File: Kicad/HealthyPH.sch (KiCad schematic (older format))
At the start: 13 parts, among them P1 CONN_8

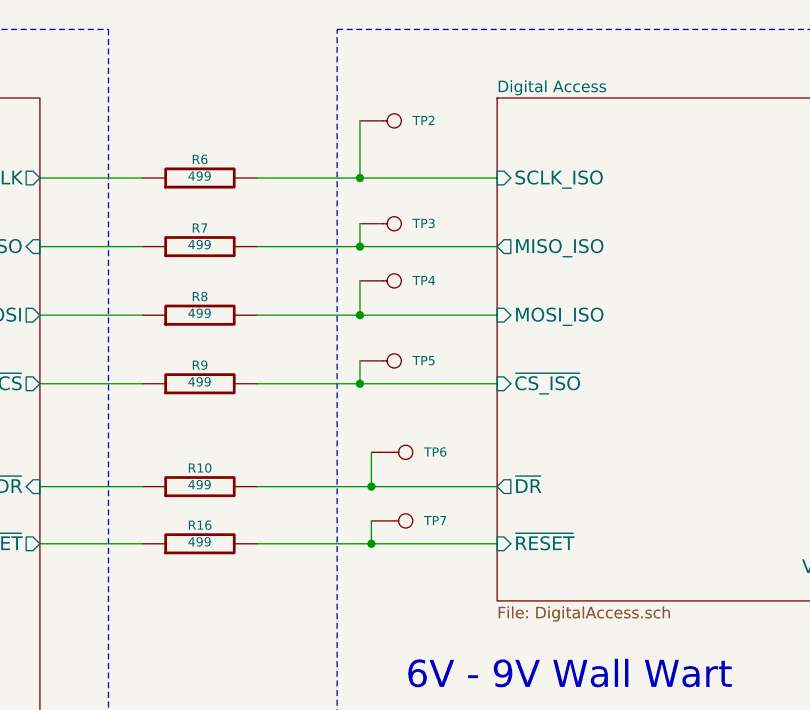
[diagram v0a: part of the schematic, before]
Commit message: updated with changes for pH volt testing in mcp3901
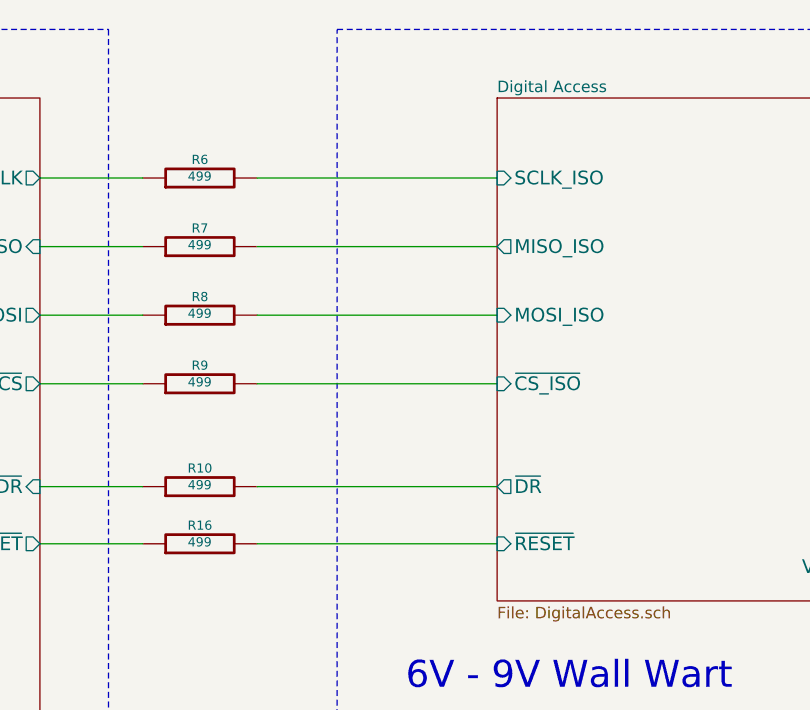
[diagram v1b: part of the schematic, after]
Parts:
- removed TP2, TP3, TP4, TP5, TP6, TP7: CONN_1, symbol CONN_1
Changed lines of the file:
@@
 Sheet 1 7
 Title ""
-Date "15 sep 2014"
+Date "11 oct 2014"
 Rev ""
 Comp ""
@@
 	1    0    0    -1
 $EndComp
-$Comp
-L CONN_1 TP2
-U 1 1 53F5DD37
-P 4250 1000
-F 0 "TP2" H 4330 1000 40  0000 L CNN
-F 1 "CONN_1" H 4250 1055 30  0001 C CNN
-F 2 "" H 4250 1000 60  0000 C CNN
-F 3 "" H 4250 1000 60  0000 C CNN
-	1    4250 1000
-	1    0    0    -1
-$EndComp
-$Comp
-L CONN_1 TP3
-U 1 1 53F5DE71
-P 4250 1450
-F 0 "TP3" H 4330 1450 40  0000 L CNN
-F 1 "CONN_1" H 4250 1505 30  0001 C CNN
-F 2 "" H 4250 1450 60  0000 C CNN
-F 3 "" H 4250 1450 60  0000 C CNN
-	1    4250 1450
-	1    0    0    -1
-$EndComp
-$Comp
-L CONN_1 TP4
-U 1 1 53F5DF29
-P 4250 1700
-F 0 "TP4" H 4330 1700 40  0000 L CNN
-F 1 "CONN_1" H 4250 1755 30  0001 C CNN
-F 2 "" H 4250 1700 60  0000 C CNN
-F 3 "" H 4250 1700 60  0000 C CNN
-	1    4250 1700
-	1    0    0    -1
-$EndComp
-$Comp
-L CONN_1 TP5
-U 1 1 53F5DFE3
-P 4250 2050
-F 0 "TP5" H 4330 2050 40  0000 L CNN
-F 1 "CONN_1" H 4250 2105 30  0001 C CNN
-F 2 "" H 4250 2050 60  0000 C CNN
-F 3 "" H 4250 2050 60  0000 C CNN
-	1    4250 2050
-	1    0    0    -1
-$EndComp
-$Comp
-L CONN_1 TP6
-U 1 1 53F5E09F
-P 4300 2450
-F 0 "TP6" H 4380 2450 40  0000 L CNN
-F 1 "CONN_1" H 4300 2505 30  0001 C CNN
-F 2 "" H 4300 2450 60  0000 C CNN
-F 3 "" H 4300 2450 60  0000 C CNN
-	1    4300 2450
-	1    0    0    -1
-$EndComp
-$Comp
-L CONN_1 TP7
-U 1 1 53F5E15D
-P 4300 2750
-F 0 "TP7" H 4380 2750 40  0000 L CNN
-F 1 "CONN_1" H 4300 2805 30  0001 C CNN
-F 2 "" H 4300 2750 60  0000 C CNN
-F 3 "" H 4300 2750 60  0000 C CNN
-	1    4300 2750
-	1    0    0    -1
-$EndComp
 Wire Wire Line
 	6650 1000 7250 1000
@@
 Wire Wire Line
 	7250 1400 6800 1400
-Wire Wire Line
-	4100 1000 4100 1250
-Connection ~ 4100 1250
-Wire Wire Line
-	4100 1450 4100 1550
-Connection ~ 4100 1550
-Wire Wire Line
-	4100 1700 4100 1850
-Connection ~ 4100 1850
-Wire Wire Line
-	4100 2050 4100 2150
-Connection ~ 4100 2150
-Wire Wire Line
-	4150 2450 4150 2600
-Connection ~ 4150 2600
-Wire Wire Line
-	4150 2750 4150 2850
 Wire Wire Line
 	10150 2600 10150 1400
@@
 Wire Wire Line
 	3650 2850 4700 2850
-Connection ~ 4150 2850
 Wire Wire Line
 	6800 2600 10150 2600

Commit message: Ready for Rev3 First layout review
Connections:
- net Digital Access/V+_WallWart: now also P1.3 (P3); no longer P1.4 (P4)
- net Temperature/10K Therm: now also P1.4 (P4); no longer P1.3 (P3)
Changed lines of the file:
@@
 Sheet 1 7
 Title ""
-Date "11 oct 2014"
+Date "18 oct 2014"
 Rev ""
 Comp ""
@@
 	9150 2150 10000 2150
 Wire Wire Line
-	10000 2150 10000 1300
-Wire Wire Line
-	10000 1300 10700 1300
-Wire Wire Line
 	10300 1500 10300 4000
 Wire Wire Line
@@
 	7250 1400 6800 1400
 Wire Wire Line
-	10150 2600 10150 1400
-Wire Wire Line
-	10150 1400 10700 1400
+	10150 1300 10150 2600
 $Sheet
 S 7250 800  1900 700
@@
 	3650 2850 4700 2850
 Wire Wire Line
-	6800 2600 10150 2600
+	10150 2600 6800 2600
 Connection ~ 6800 2600
+Wire Wire Line
+	10150 1300 10700 1300
+Wire Wire Line
+	10700 1400 10000 1400
+Wire Wire Line
+	10000 1400 10000 2150
 $EndSCHEMATC

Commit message: updated based on feedback. Ready for second review
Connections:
- net Digital Access/V+_WallWart: no longer P1.3 (P3)
- net Temperature/10K Therm: now also P1.3 (P3); no longer P1.4 (P4)
- net pH/pH_Probe_GND: now also P1.1 (P1); no longer P1.2 (P2)
- net pH/pH_Probe_V: now also P1.2 (P2); no longer P1.1 (P1)
- new net Temperature/V+_WallWart_Out: P1.4 (P4)
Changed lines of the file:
@@
 Sheet 1 7
 Title ""
-Date "18 oct 2014"
+Date "21 oct 2014"
 Rev ""
 Comp ""
@@
 F1 "WallWart.sch" 50
 F2 "V+_WallWart" O L 7250 3150 60
-$EndSheet
-$Sheet
-S 800  900  1900 3900
-U 53DCD805
-F0 "Arduino" 50
-F1 "Arduino.sch" 50
-F2 "SCLK" O R 2700 1250 60
-F3 "MISO" I R 2700 1550 60
-F4 "MOSI" O R 2700 1850 60
-F5 "~CS" O R 2700 2150 60
-F6 "~RESET" O R 2700 2850 60
-F7 "~DR" I R 2700 2600 60
-F8 "V+_ARD" O R 2700 3900 60
-F9 "GND_ARD" I R 2700 4100 60
-F10 "PumpUp" O R 2700 4350 60
-F11 "PumpDown" O R 2700 4600 60
 $EndSheet
 Text Notes 2900 4900 0    118  ~ 0
@@
 F3 "Therm+" O L 7250 2050 60
 F4 "Therm-" O L 7250 2200 60
+F5 "V+_WallWart" I L 7250 2350 60
+F6 "V+_WallWart_Out" O R 9150 2350 60
 $EndSheet
 $Sheet
@@
 	3650 2600 4700 2600
 Wire Wire Line
-	9150 1200 10700 1200
-Wire Wire Line
-	9150 2150 10000 2150
+	10000 2150 9150 2150
 Wire Wire Line
 	10300 1500 10300 4000
@@
 Wire Wire Line
 	7250 1400 6800 1400
-Wire Wire Line
-	10150 1300 10150 2600
 $Sheet
 S 7250 800  1900 700
@@
 F3 "ph_ADC_IN+" I L 7250 1000 60
 F4 "pH_ADC_IN-" I L 7250 1200 60
-F5 "pH_Probe_V" I R 9150 1000 60
-F6 "pH_Probe_GND" I R 9150 1200 60
-$EndSheet
-Wire Wire Line
-	9150 1000 10600 1000
-Wire Wire Line
-	10600 1000 10600 1100
-Wire Wire Line
-	10600 1100 10700 1100
+F5 "pH_Probe_V" I R 9150 1200 60
+F6 "pH_Probe_GND" I R 9150 1000 60
+$EndSheet
 $Sheet
 S 4700 900  1950 2200
@@
 	3650 2850 4700 2850
 Wire Wire Line
-	10150 2600 6800 2600
-Connection ~ 6800 2600
-Wire Wire Line
-	10150 1300 10700 1300
-Wire Wire Line
-	10700 1400 10000 1400
-Wire Wire Line
-	10000 1400 10000 2150
+	10100 2350 9150 2350
+Wire Wire Line
+	7250 2350 6800 2350
+Connection ~ 6800 2350
+Wire Wire Line
+	9150 1200 10700 1200
+Wire Wire Line
+	9150 1000 10450 1000
+Wire Wire Line
+	10100 2350 10100 1400
+Wire Wire Line
+	10100 1400 10700 1400
+Wire Wire Line
+	10000 2150 10000 1300
+Wire Wire Line
+	10000 1300 10700 1300
+Wire Wire Line
+	10450 1000 10450 1100
+Wire Wire Line
+	10450 1100 10700 1100
+$Sheet
+S 800  900  1900 3900
+U 53DCD805
+F0 "Arduino" 50
+F1 "Arduino.sch" 50
+F2 "SCLK" O R 2700 1250 60
+F3 "MISO" I R 2700 1550 60
+F4 "MOSI" O R 2700 1850 60
+F5 "~CS" O R 2700 2150 60
+F6 "V+_ARD" O R 2700 3900 60
+F7 "GND_ARD" I R 2700 4100 60
+F8 "PumpUp" O R 2700 4350 60
+F9 "PumpDown" O R 2700 4600 60
+F10 "~RESET" O R 2700 2850 60
+F11 "~DR" I R 2700 2600 60
+$EndSheet
 $EndSCHEMATC

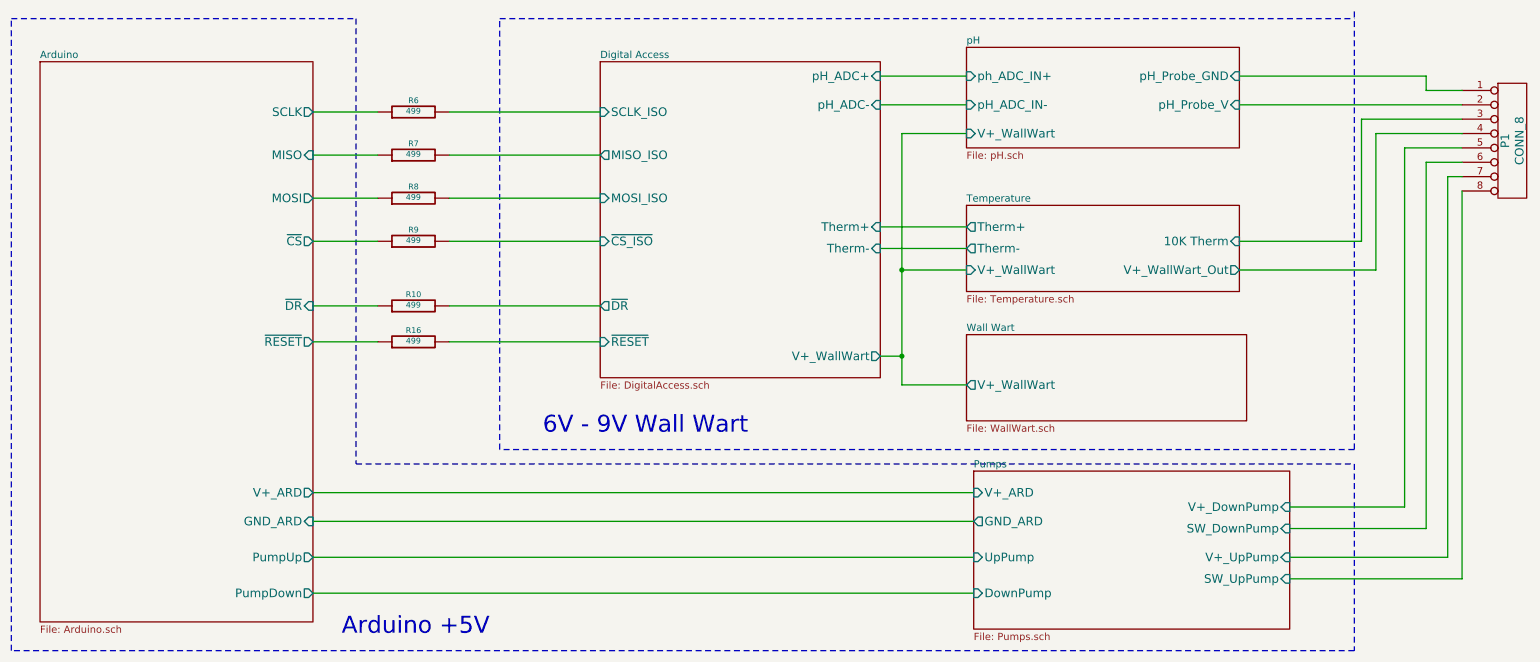
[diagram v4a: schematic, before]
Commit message: first pass changing ADC
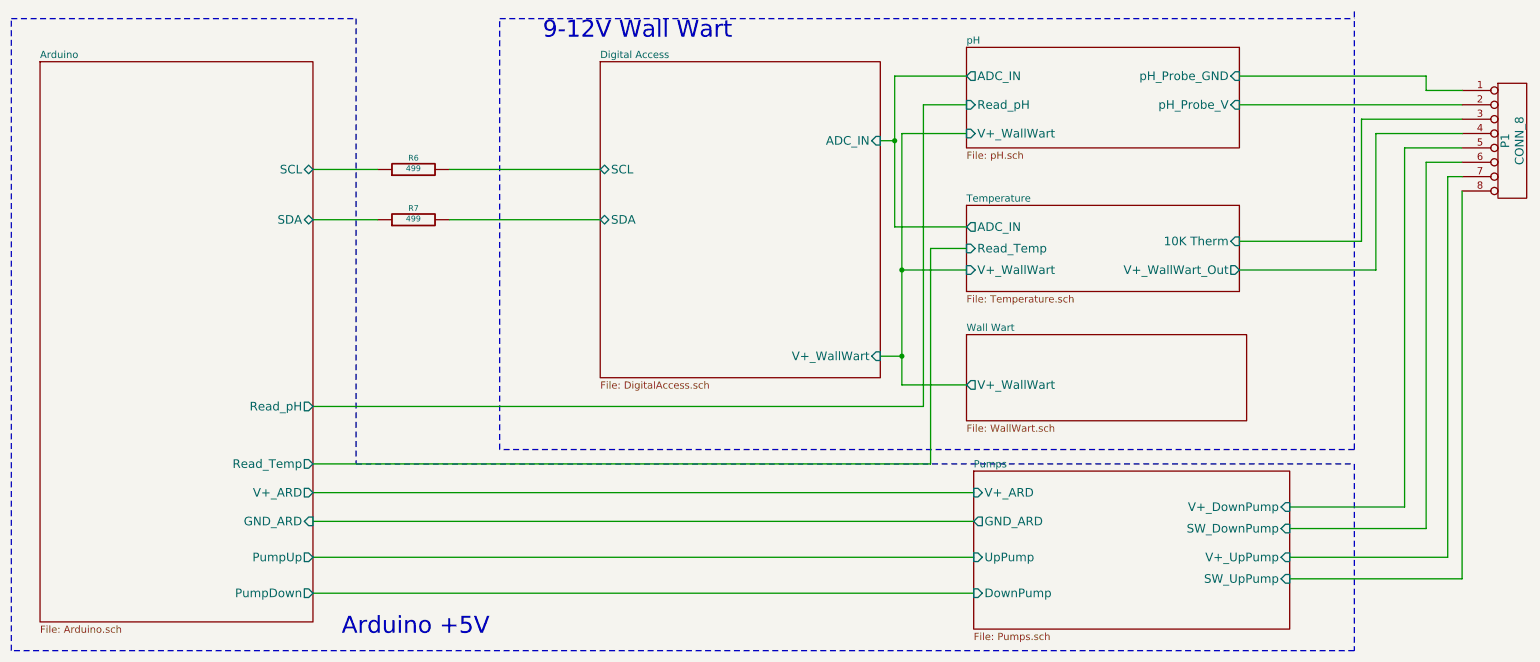
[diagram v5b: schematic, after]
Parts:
- removed R10, R16, R8, R9: 499, ~, symbol R
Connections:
- net Arduino/MISO renamed Arduino/SDA
- net Arduino/SCLK renamed Arduino/SCL
- net Digital Access/MISO_ISO renamed Digital Access/SDA
- net Digital Access/SCLK_ISO renamed Digital Access/SCL
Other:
- note added: "9-12V Wall Wart"
- note removed: "6V - 9V Wall Wart"
- moved on the sheet: R6, R7
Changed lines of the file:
@@
 Sheet 1 7
 Title ""
-Date "10 nov 2014"
+Date "11 nov 2014"
 Rev ""
 Comp ""
@@
 Text Notes 2900 4900 0    118  ~ 0
 Arduino +5V
-Text Notes 4300 3500 0    118  ~ 0
-6V - 9V Wall Wart
+Text Notes 4300 750  0    118  ~ 0
+9-12V Wall Wart
 $Comp
 L R R6
 U 1 1 53E4B553
-P 3400 1250
-F 0 "R6" V 3480 1250 40  0000 C CNN
-F 1 "499" V 3407 1251 40  0000 C CNN
-F 2 "~" V 3330 1250 30  0000 C CNN
-F 3 "~" H 3400 1250 30  0000 C CNN
-	1    3400 1250
+P 3400 1650
+F 0 "R6" V 3480 1650 40  0000 C CNN
+F 1 "499" V 3407 1651 40  0000 C CNN
+F 2 "~" V 3330 1650 30  0000 C CNN
+F 3 "~" H 3400 1650 30  0000 C CNN
+	1    3400 1650
 	0    -1   -1   0
 $EndComp
@@
 L R R7
 U 1 1 53E4B560
-P 3400 1550
-F 0 "R7" V 3480 1550 40  0000 C CNN
-F 1 "499" V 3407 1551 40  0000 C CNN
-F 2 "~" V 3330 1550 30  0000 C CNN
-F 3 "~" H 3400 1550 30  0000 C CNN
-	1    3400 1550
-	0    -1   -1   0
-$EndComp
-$Comp
-L R R8
-U 1 1 53E4B566
-P 3400 1850
-F 0 "R8" V 3480 1850 40  0000 C CNN
-F 1 "499" V 3407 1851 40  0000 C CNN
-F 2 "~" V 3330 1850 30  0000 C CNN
-F 3 "~" H 3400 1850 30  0000 C CNN
-	1    3400 1850
-	0    -1   -1   0
-$EndComp
-$Comp
-L R R9
-U 1 1 53E4B56C
-P 3400 2150
-F 0 "R9" V 3480 2150 40  0000 C CNN
-F 1 "499" V 3407 2151 40  0000 C CNN
-F 2 "~" V 3330 2150 30  0000 C CNN
-F 3 "~" H 3400 2150 30  0000 C CNN
-	1    3400 2150
-	0    -1   -1   0
-$EndComp
-$Comp
-L R R10
-U 1 1 53E4B572
-P 3400 2600
-F 0 "R10" V 3480 2600 40  0000 C CNN
-F 1 "499" V 3407 2601 40  0000 C CNN
-F 2 "~" V 3330 2600 30  0000 C CNN
-F 3 "~" H 3400 2600 30  0000 C CNN
-	1    3400 2600
+P 3400 2000
+F 0 "R7" V 3480 2000 40  0000 C CNN
+F 1 "499" V 3407 2001 40  0000 C CNN
+F 2 "~" V 3330 2000 30  0000 C CNN
+F 3 "~" H 3400 2000 30  0000 C CNN
+	1    3400 2000
 	0    -1   -1   0
 $EndComp
@@
 F1 "Temperature.sch" 50
 F2 "10K Therm" I R 9150 2150 60
-F3 "Therm+" O L 7250 2050 60
-F4 "Therm-" O L 7250 2200 60
-F5 "V+_WallWart" I L 7250 2350 60
-F6 "V+_WallWart_Out" O R 9150 2350 60
+F3 "V+_WallWart" I L 7250 2350 60
+F4 "V+_WallWart_Out" O R 9150 2350 60
+F5 "ADC_IN" O L 7250 2050 60
+F6 "Read_Temp" I L 7250 2200 60
 $EndSheet
 $Sheet
@@
 $EndComp
 Wire Wire Line
-	6650 1000 7250 1000
-Wire Wire Line
-	6650 1200 7250 1200
-Wire Wire Line
 	6800 1400 6800 3150
 Wire Wire Line
@@
 	600  600  3000 600
 Wire Wire Line
-	3650 1250 4700 1250
-Wire Wire Line
-	3650 1550 4700 1550
-Wire Wire Line
-	3650 1850 4700 1850
-Wire Wire Line
-	3650 2150 4700 2150
-Wire Wire Line
-	3650 2600 4700 2600
+	3650 1650 4700 1650
+Wire Wire Line
+	3650 2000 4700 2000
 Wire Wire Line
 	10000 2150 9150 2150
@@
 	10700 4500 9500 4500
 Wire Wire Line
-	3150 1250 2700 1250
-Wire Wire Line
-	3150 1550 2700 1550
-Wire Wire Line
-	2700 1850 3150 1850
-Wire Wire Line
-	3150 2150 2700 2150
-Wire Wire Line
-	2700 2600 3150 2600
+	3150 1650 2700 1650
+Wire Wire Line
+	3150 2000 2700 2000
 Wire Wire Line
 	7250 1400 6800 1400
@@
 F1 "pH.sch" 50
 F2 "V+_WallWart" I L 7250 1400 60
-F3 "ph_ADC_IN+" I L 7250 1000 60
-F4 "pH_ADC_IN-" I L 7250 1200 60
-F5 "pH_Probe_V" I R 9150 1200 60
-F6 "pH_Probe_GND" I R 9150 1000 60
+F3 "pH_Probe_V" I R 9150 1200 60
+F4 "pH_Probe_GND" I R 9150 1000 60
+F5 "ADC_IN" O L 7250 1000 60
+F6 "Read_pH" I L 7250 1200 60
+$EndSheet
+Wire Wire Line
+	10100 2350 9150 2350
+Wire Wire Line
+	7250 2350 6800 2350
+Connection ~ 6800 2350
+Wire Wire Line
+	9150 1200 10700 1200
+Wire Wire Line
+	9150 1000 10450 1000
+Wire Wire Line
+	10100 2350 10100 1400
+Wire Wire Line
+	10100 1400 10700 1400
+Wire Wire Line
+	10000 2150 10000 1300
+Wire Wire Line
+	10000 1300 10700 1300
+Wire Wire Line
+	10450 1000 10450 1100
+Wire Wire Line
+	10450 1100 10700 1100
+$Sheet
+S 800  900  1900 3900
+U 53DCD805
+F0 "Arduino" 50
+F1 "Arduino.sch" 50
+F2 "V+_ARD" O R 2700 3900 60
+F3 "GND_ARD" I R 2700 4100 60
+F4 "PumpUp" O R 2700 4350 60
+F5 "PumpDown" O R 2700 4600 60
+F6 "SDA" B R 2700 2000 60
+F7 "SCL" B R 2700 1650 60
+F8 "Read_pH" O R 2700 3300 60
+F9 "Read_Temp" O R 2700 3700 60
 $EndSheet
 $Sheet
@@
 F0 "Digital Access" 50
 F1 "DigitalAccess.sch" 50
-F2 "~RESET" I L 4700 2850 60
-F3 "~DR" O L 4700 2600 60
-F4 "pH_ADC+" I R 6650 1000 60
-F5 "pH_ADC-" I R 6650 1200 60
-F6 "V+_WallWart" O R 6650 2950 60
-F7 "MOSI_ISO" I L 4700 1850 60
-F8 "MISO_ISO" O L 4700 1550 60
-F9 "SCLK_ISO" I L 4700 1250 60
-F10 "~CS_ISO" I L 4700 2150 60
-F11 "Therm+" I R 6650 2050 60
-F12 "Therm-" I R 6650 2200 60
-$EndSheet
-Wire Wire Line
-	6650 2200 7250 2200
-Wire Wire Line
-	6650 2050 7250 2050
-$Comp
-L R R16
-U 1 1 54142348
-P 3400 2850
-F 0 "R16" V 3480 2850 40  0000 C CNN
-F 1 "499" V 3407 2851 40  0000 C CNN
-F 2 "~" V 3330 2850 30  0000 C CNN
-F 3 "~" H 3400 2850 30  0000 C CNN
-	1    3400 2850
-	0    -1   -1   0
-$EndComp
-Wire Wire Line
-	2700 2850 3150 2850
-Wire Wire Line
-	3650 2850 4700 2850
-Wire Wire Line
-	10100 2350 9150 2350
-Wire Wire Line
-	7250 2350 6800 2350
-Connection ~ 6800 2350
-Wire Wire Line
-	9150 1200 10700 1200
-Wire Wire Line
-	9150 1000 10450 1000
-Wire Wire Line
-	10100 2350 10100 1400
-Wire Wire Line
-	10100 1400 10700 1400
-Wire Wire Line
-	10000 2150 10000 1300
-Wire Wire Line
-	10000 1300 10700 1300
-Wire Wire Line
-	10450 1000 10450 1100
-Wire Wire Line
-	10450 1100 10700 1100
-$Sheet
-S 800  900  1900 3900
-U 53DCD805
-F0 "Arduino" 50
-F1 "Arduino.sch" 50
-F2 "SCLK" O R 2700 1250 60
-F3 "MISO" I R 2700 1550 60
-F4 "MOSI" O R 2700 1850 60
-F5 "~CS" O R 2700 2150 60
-F6 "V+_ARD" O R 2700 3900 60
-F7 "GND_ARD" I R 2700 4100 60
-F8 "PumpUp" O R 2700 4350 60
-F9 "PumpDown" O R 2700 4600 60
-F10 "~RESET" O R 2700 2850 60
-F11 "~DR" I R 2700 2600 60
-$EndSheet
+F2 "V+_WallWart" I R 6650 2950 60
+F3 "SCL" B L 4700 1650 60
+F4 "SDA" B L 4700 2000 60
+F5 "ADC_IN" I R 6650 1450 60
+$EndSheet
+Wire Wire Line
+	2700 3300 6950 3300
+Wire Wire Line
+	6950 3300 6950 1200
+Wire Wire Line
+	2700 3700 7000 3700
+Wire Wire Line
+	7000 3700 7000 2200
+Wire Wire Line
+	6950 1200 7250 1200
+Wire Wire Line
+	7000 2200 7250 2200
+Wire Wire Line
+	7250 1000 6750 1000
+Wire Wire Line
+	6750 1000 6750 2050
+Wire Wire Line
+	6750 2050 7250 2050
+Wire Wire Line
+	6650 1450 6750 1450
+Connection ~ 6750 1450
 $EndSCHEMATC

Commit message: prior to using Arduino ADC
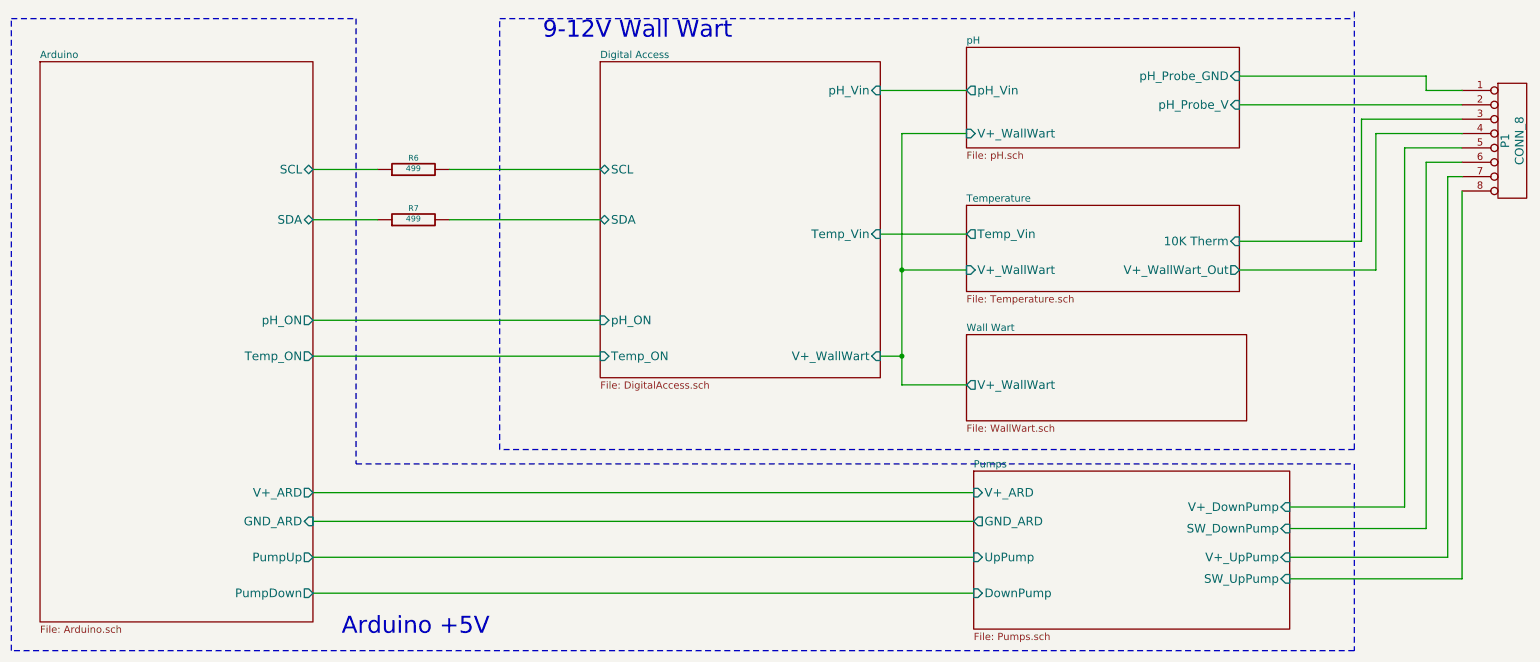
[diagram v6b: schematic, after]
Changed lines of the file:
@@
 Sheet 1 7
 Title ""
-Date "11 nov 2014"
+Date "12 nov 2014"
 Rev ""
 Comp ""
@@
 F3 "V+_WallWart" I L 7250 2350 60
 F4 "V+_WallWart_Out" O R 9150 2350 60
-F5 "ADC_IN" O L 7250 2050 60
-F6 "Read_Temp" I L 7250 2200 60
+F5 "Temp_Vin" O L 7250 2100 60
 $EndSheet
 $Sheet
@@
 Wire Wire Line
 	7250 1400 6800 1400
-$Sheet
-S 7250 800  1900 700
-U 53C9635B
-F0 "pH" 50
-F1 "pH.sch" 50
-F2 "V+_WallWart" I L 7250 1400 60
-F3 "pH_Probe_V" I R 9150 1200 60
-F4 "pH_Probe_GND" I R 9150 1000 60
-F5 "ADC_IN" O L 7250 1000 60
-F6 "Read_pH" I L 7250 1200 60
-$EndSheet
 Wire Wire Line
 	10100 2350 9150 2350
@@
 F6 "SDA" B R 2700 2000 60
 F7 "SCL" B R 2700 1650 60
-F8 "Read_pH" O R 2700 3300 60
-F9 "Read_Temp" O R 2700 3700 60
+F8 "pH_ON" O R 2700 2700 60
+F9 "Temp_ON" O R 2700 2950 60
 $EndSheet
 $Sheet
@@
 F3 "SCL" B L 4700 1650 60
 F4 "SDA" B L 4700 2000 60
-F5 "ADC_IN" I R 6650 1450 60
-$EndSheet
-Wire Wire Line
-	2700 3300 6950 3300
-Wire Wire Line
-	6950 3300 6950 1200
-Wire Wire Line
-	2700 3700 7000 3700
-Wire Wire Line
-	7000 3700 7000 2200
-Wire Wire Line
-	6950 1200 7250 1200
-Wire Wire Line
-	7000 2200 7250 2200
-Wire Wire Line
-	7250 1000 6750 1000
-Wire Wire Line
-	6750 1000 6750 2050
-Wire Wire Line
-	6750 2050 7250 2050
-Wire Wire Line
-	6650 1450 6750 1450
-Connection ~ 6750 1450
+F5 "pH_Vin" I R 6650 1100 60
+F6 "Temp_Vin" I R 6650 2100 60
+F7 "pH_ON" I L 4700 2700 60
+F8 "Temp_ON" I L 4700 2950 60
+$EndSheet
+$Sheet
+S 7250 800  1900 700
+U 53C9635B
+F0 "pH" 50
+F1 "pH.sch" 50
+F2 "V+_WallWart" I L 7250 1400 60
+F3 "pH_Probe_V" I R 9150 1200 60
+F4 "pH_Probe_GND" I R 9150 1000 60
+F5 "pH_Vin" O L 7250 1100 60
+$EndSheet
+Wire Wire Line
+	7250 1100 6650 1100
+Wire Wire Line
+	7250 2100 6650 2100
+Wire Wire Line
+	2700 2700 4700 2700
+Wire Wire Line
+	4700 2950 2700 2950
 $EndSCHEMATC
